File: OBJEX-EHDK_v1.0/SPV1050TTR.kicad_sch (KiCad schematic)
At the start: 14 parts

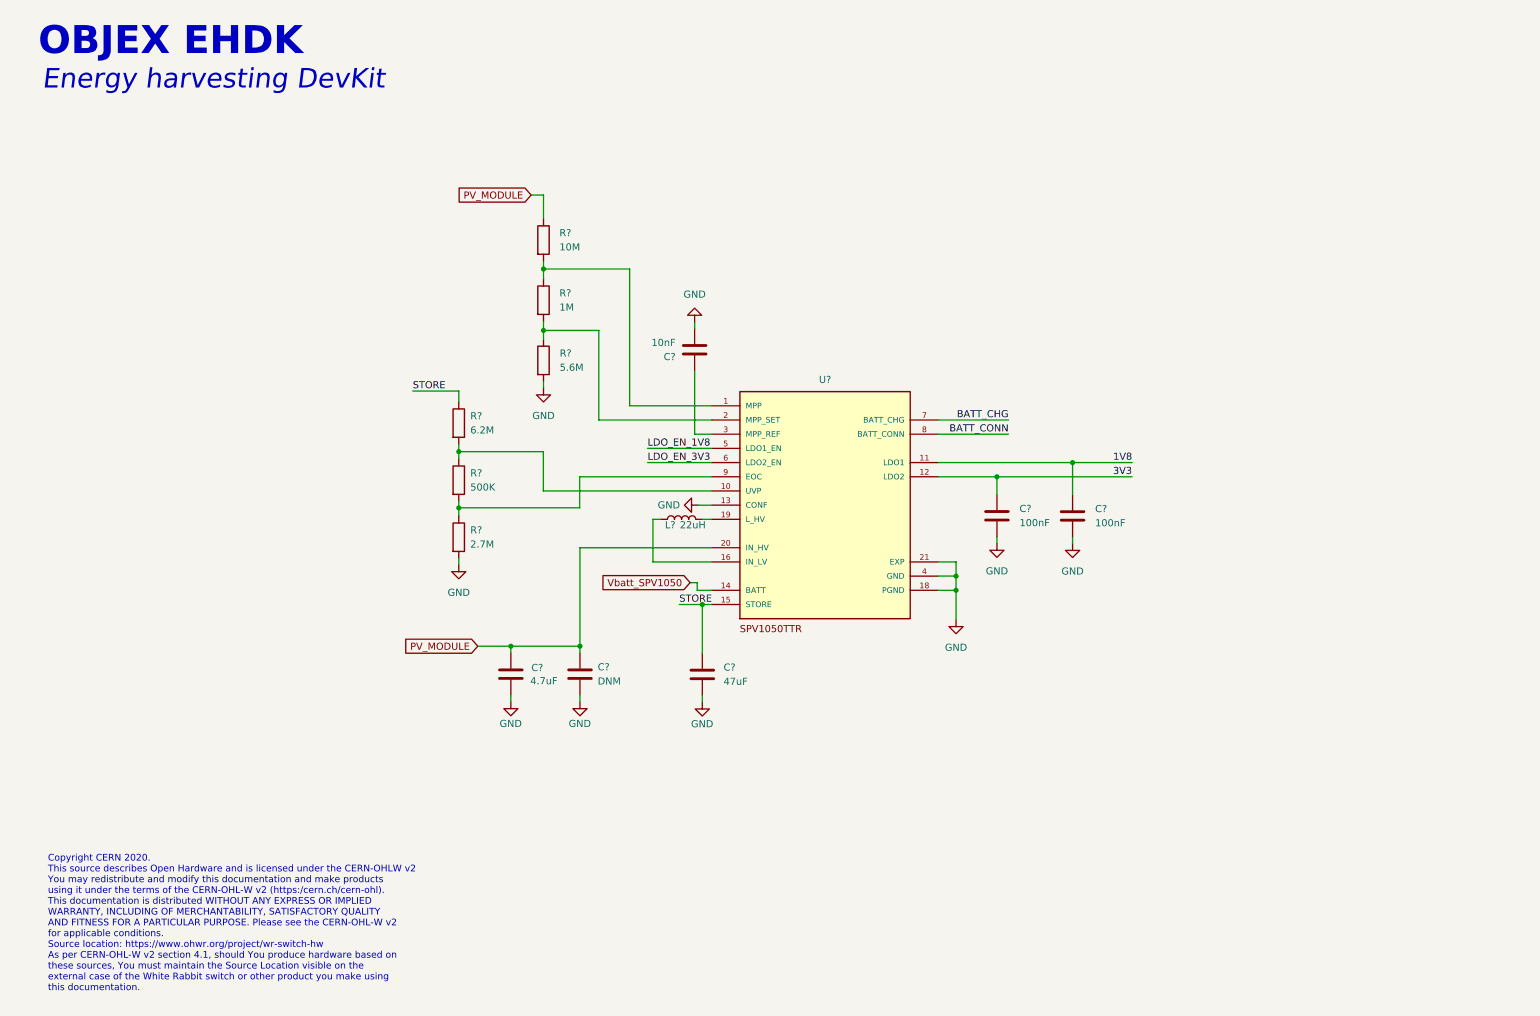
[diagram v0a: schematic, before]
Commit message: Update design, EH ICs & Battery conn
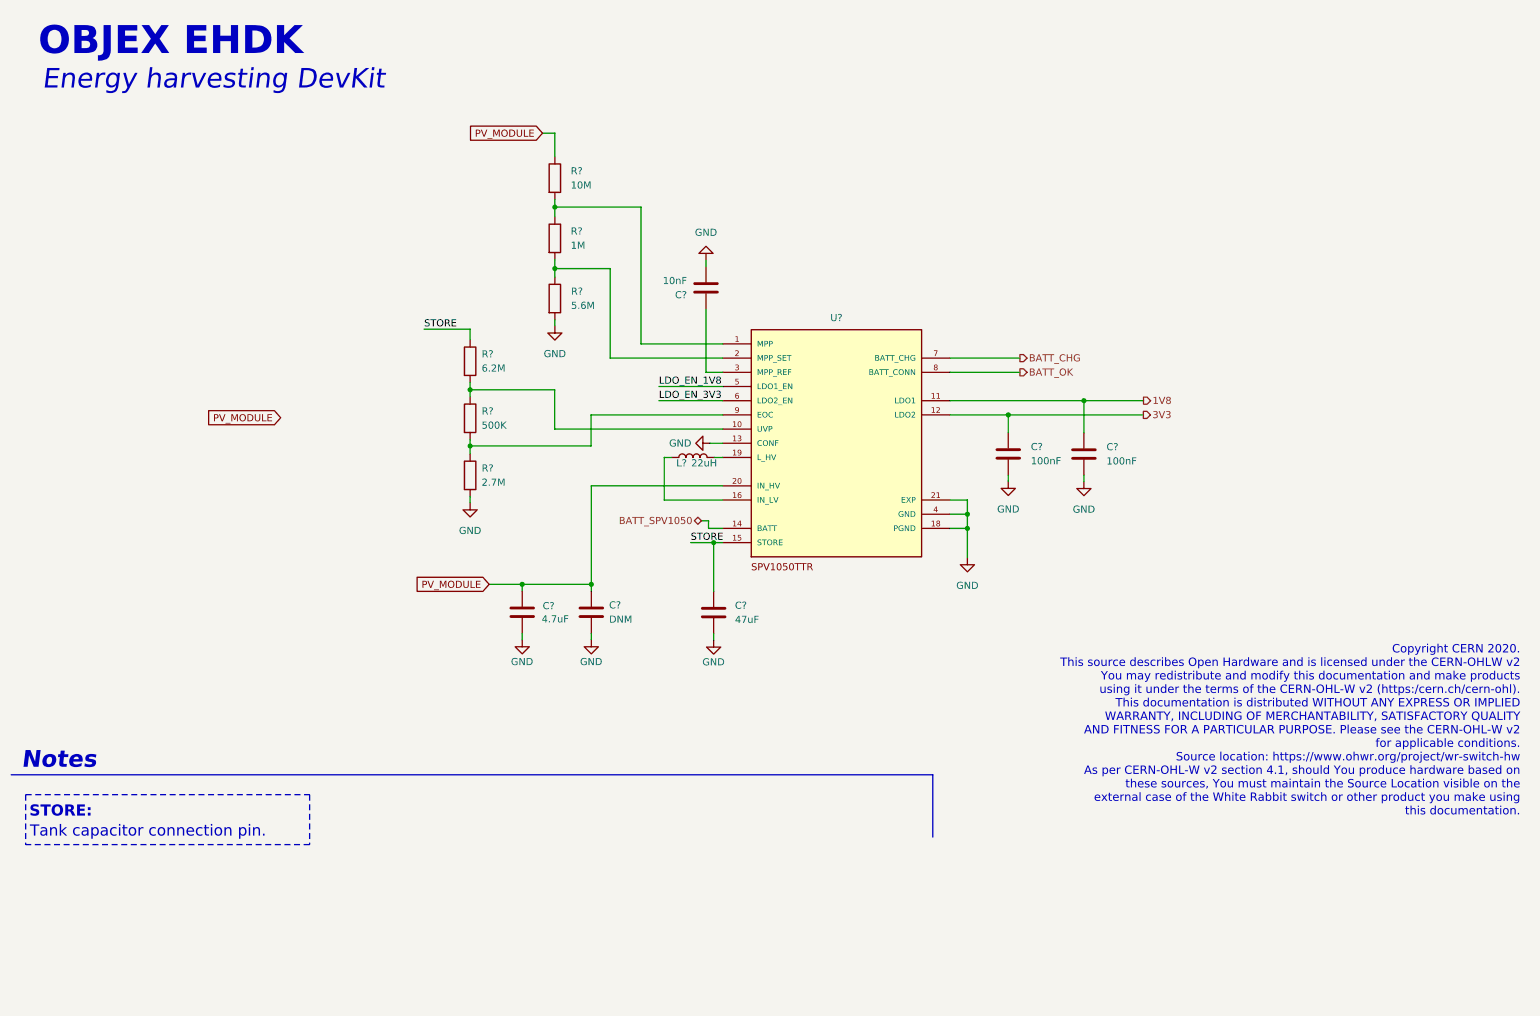
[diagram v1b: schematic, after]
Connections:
- net BATT_CONN renamed BATT_OK
- net Vbatt_SPV1050 renamed BATT_SPV1050
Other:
- note added: "Notes"
- note added: "STORE:"
- note added: "Tank capacitor connection pin."
- moved on the sheet: C?, L?, R?, U?

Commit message: update sch
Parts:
- added J?: Conn_01x05, symbol Connector_Generic:Conn_01x05
- added J?: Solar, symbol Connector_Generic:Conn_01x02
- added J?: 3V3, symbol Connector_Generic:Conn_01x02
- added J?: 1V8, symbol Connector_Generic:Conn_01x02
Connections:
- net BATT_CHG: now also J?.2 (Pin_2)
- net BATT_OK: now also J?.1 (Pin_1)
- net GND: now also J?.1 (Pin_1), J?.2 (Pin_2), J?.2 (Pin_2)
- net LDO_EN_1V8: now also J?.3 (Pin_3)
- net LDO_EN_3V3: now also J?.4 (Pin_4)
- net PV_MODULE: now also J?.2 (Pin_2)
- net STORE: now also J?.5 (Pin_5)
- net 1V8: no longer names the net of C?.1, U?.11 (LDO1)
- net 1V8: now also J?.1 (Pin_1)
- net 3V3: no longer names the net of C?.1, U?.12 (LDO2)
- net 3V3: now also J?.1 (Pin_1)
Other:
- note added: "OUTPUT"

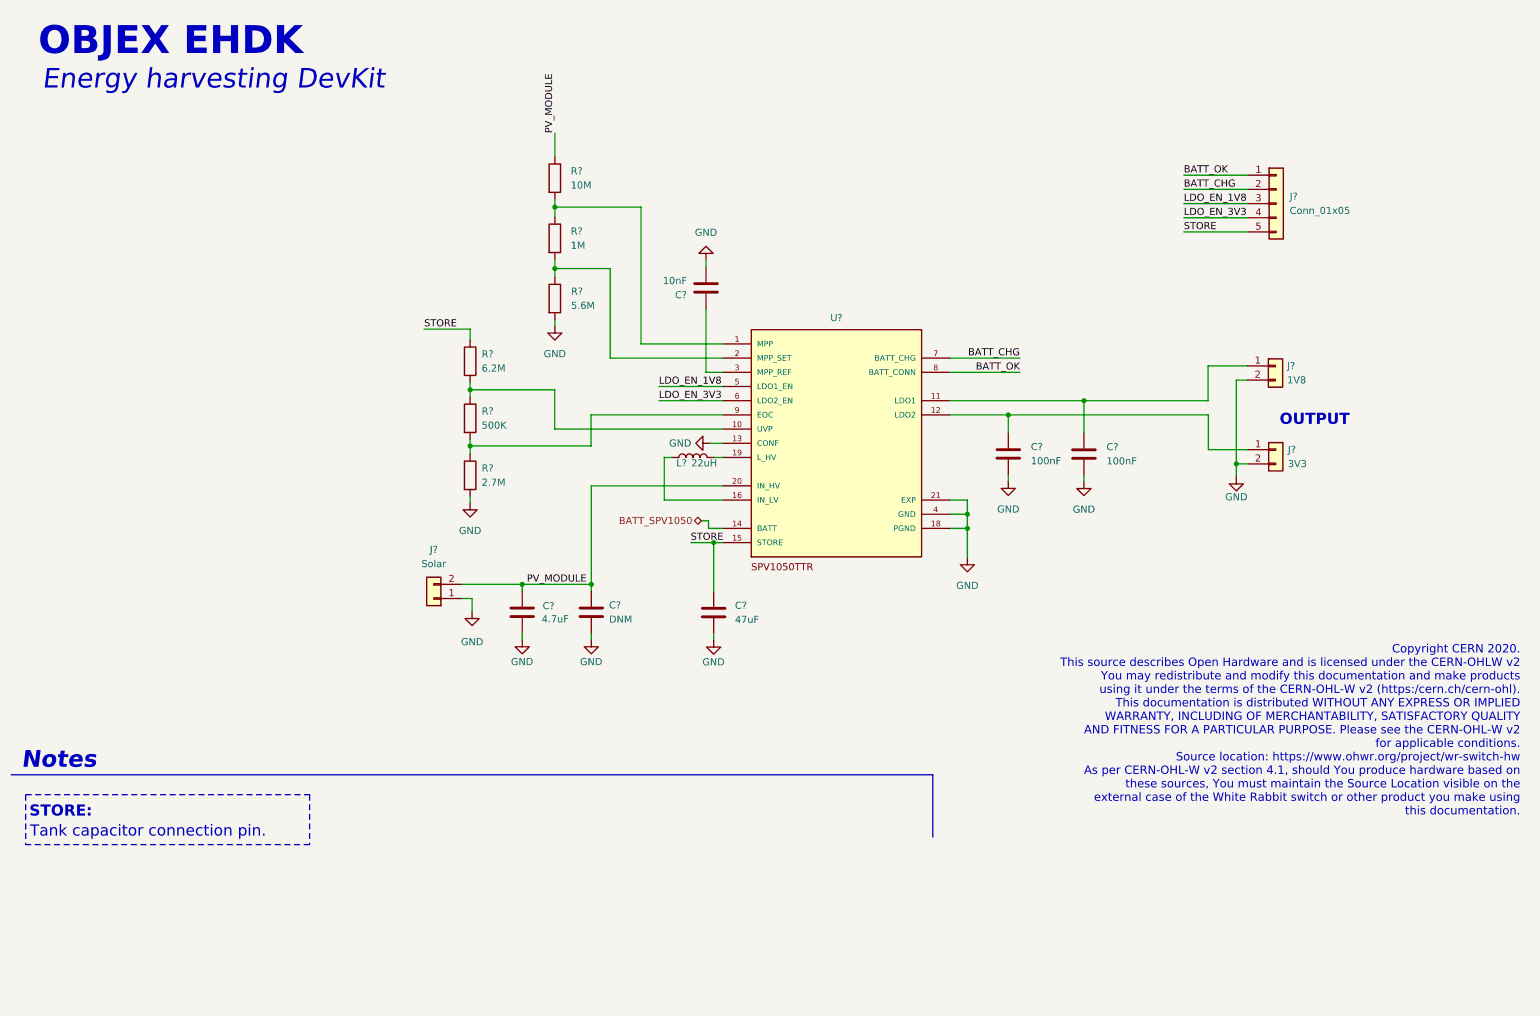
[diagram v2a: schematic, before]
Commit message: Fix, add test points
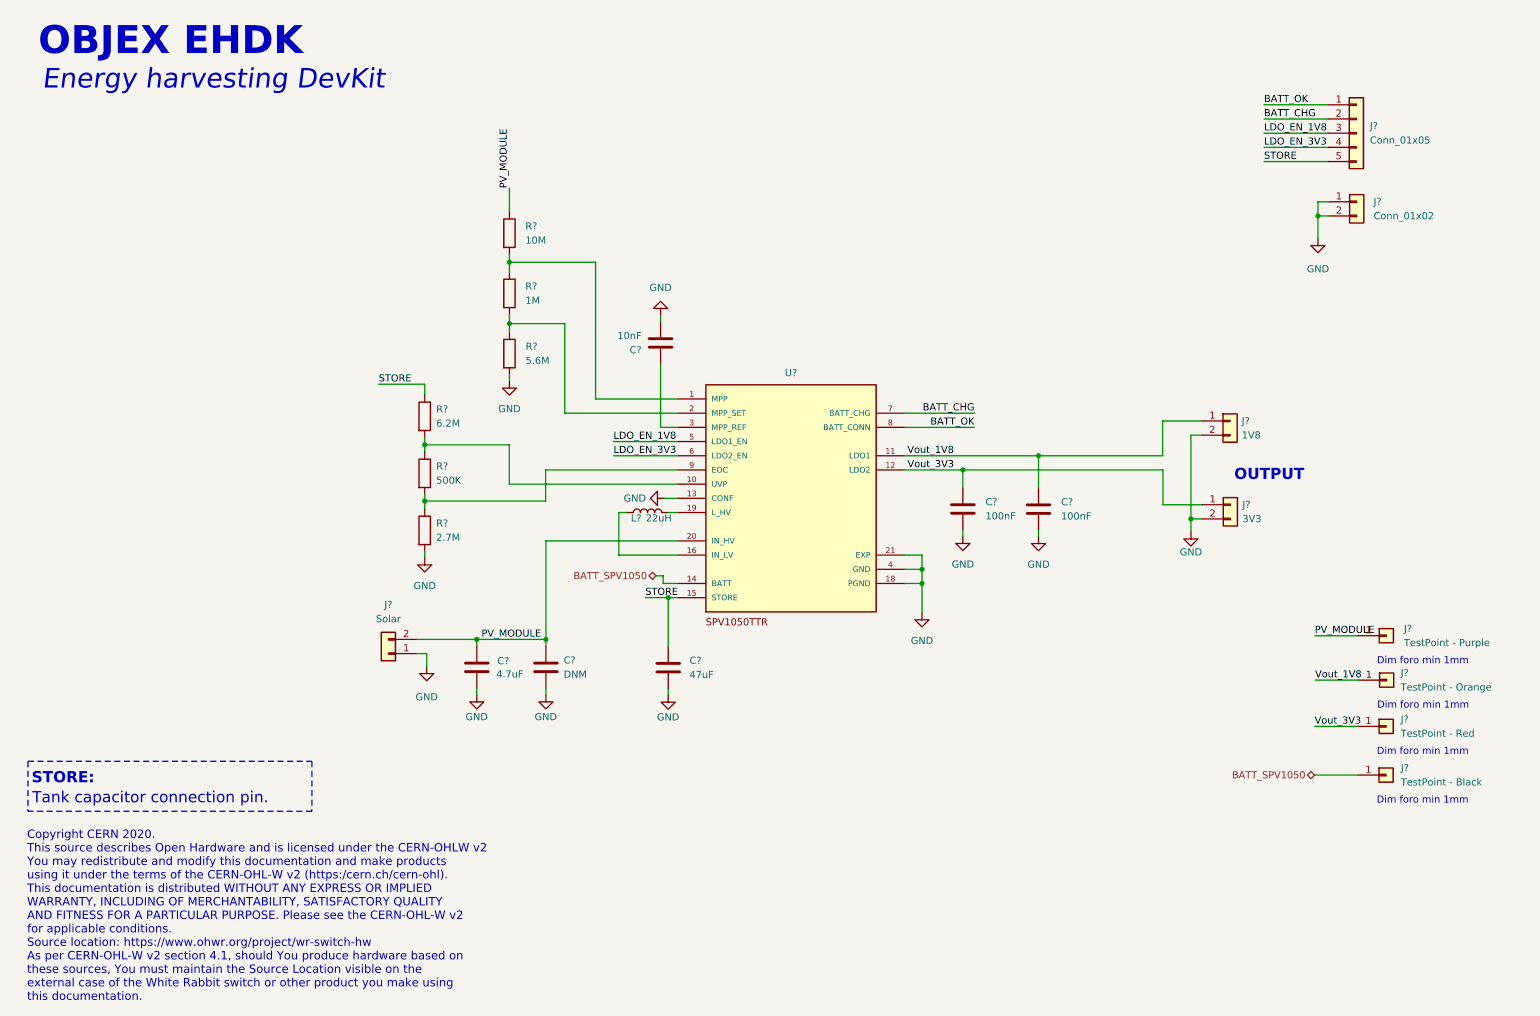
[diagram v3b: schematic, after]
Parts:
- added J?: TestPoint - Red, symbol Connector_Generic:Conn_01x01
- added J?: Conn_01x02, symbol Connector_Generic:Conn_01x02
- added J?: TestPoint - Purple, symbol Connector_Generic:Conn_01x01
- added J?: TestPoint - Orange, symbol Connector_Generic:Conn_01x01
- added J?: TestPoint - Black, symbol Connector_Generic:Conn_01x01
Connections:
- net BATT_SPV1050: now also J?.1 (Pin_1)
- net GND: now also J?.1 (Pin_1), J?.2 (Pin_2)
- net PV_MODULE: now also J?.1 (Pin_1)
- net Vout_1V8: now reaches C?.1, J?.1 (Pin_1), U?.11 (LDO1)
- net Vout_1V8: now also J?.1 (Pin_1)
- net Vout_3V3: now reaches C?.1, J?.1 (Pin_1), U?.12 (LDO2)
- net Vout_3V3: now also J?.1 (Pin_1)
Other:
- note added: "Dim foro min 1mm"
- note removed: "Notes"
- moved on the sheet: C?, J?, L?, R?, U?

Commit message: SCH Ready for first review
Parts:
- C1: renamed from C?; value 4.7uF -> 4.7uF/25V; footprint (none) -> Capacitor_SMD:C_0603_1608Metric
- C2: renamed from C?; footprint (none) -> Capacitor_SMD:C_0603_1608Metric
- C3, C5, C6: renamed from C?; footprint (none) -> Capacitor_SMD:C_0402_1005Metric
- C4: renamed from C?; value 47uF -> 47uF/10V; footprint (none) -> Capacitor_SMD:C_0805_2012Metric
- J10, J6, J7, J8: renamed from J?; footprint (none) -> Connector_PinHeader_2.54mm:PinHeader_1x02_P2.54mm_Vertical
- J11, J12, J13, J14: renamed from J?; footprint (none) -> TestPoint:TestPoint_Loop_D3.80mm_Drill2.0mm
- J9: renamed from J?; footprint (none) -> Connector_PinHeader_2.54mm:PinHeader_1x05_P2.54mm_Vertical
- L1: renamed from L?; footprint (none) -> Inductor_SMD:L_0603_1608Metric
- R1, R2, R3, R4, R5, R6: renamed from R?; footprint (none) -> Resistor_SMD:R_0603_1608Metric
- U1: renamed from U?; footprint QFN40P300X300X100-21N -> lib:QFN40P300X300X100-21N
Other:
- moved on the sheet: C1, J6

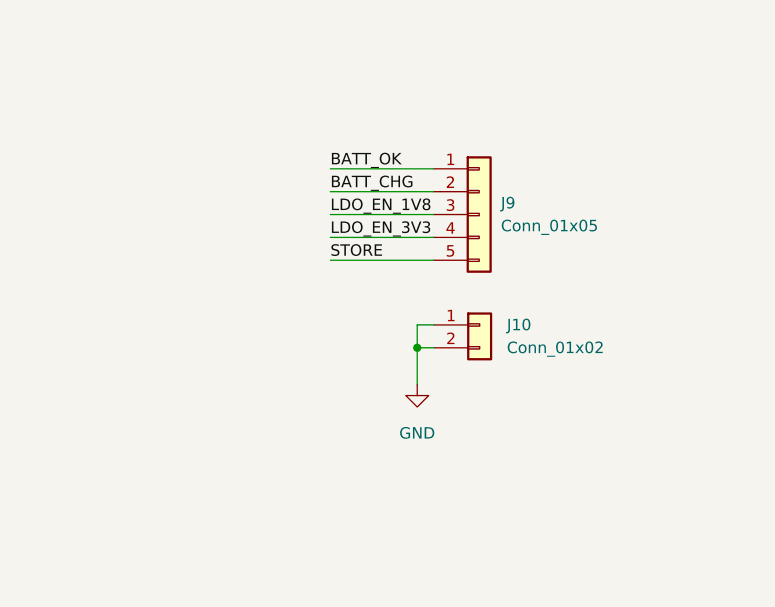
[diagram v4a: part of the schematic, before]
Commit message: SCH Ready for PCB design
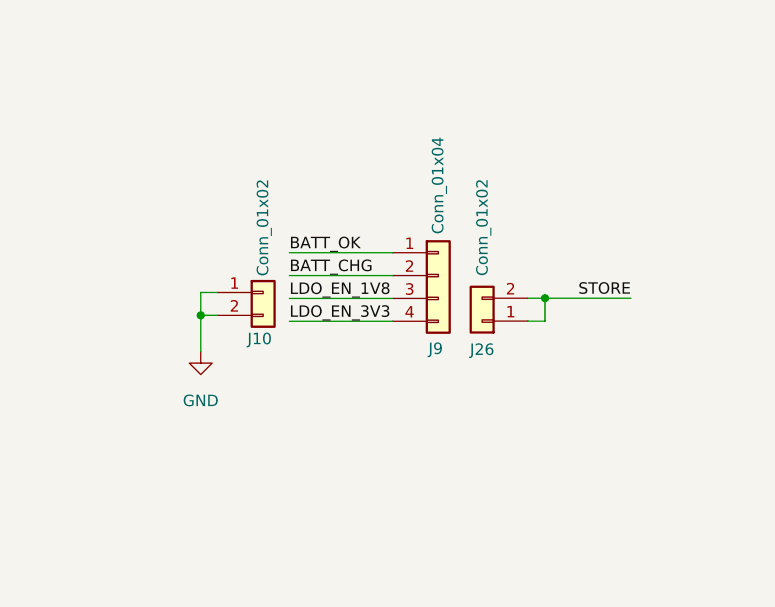
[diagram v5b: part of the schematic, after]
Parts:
- removed J9: Conn_01x05, Connector_PinHeader_2.54mm:PinHeader_1x05_P2.54mm_Vertical, symbol Connector_Generic:Conn_01x05
- added J26: Conn_01x02, Connector_PinHeader_2.54mm:PinHeader_1x02_P2.54mm_Vertical, symbol Connector_Generic:Conn_01x02
- added J9: Conn_01x04, Connector_PinHeader_2.54mm:PinHeader_1x04_P2.54mm_Vertical, symbol Connector_Generic:Conn_01x04
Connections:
- net BATT_CHG: now also J9.2 (Pin_2)
- net BATT_OK: now also J9.1 (Pin_1)
- net LDO_EN_1V8: now also J9.3 (Pin_3)
- net LDO_EN_3V3: now also J9.4 (Pin_4)
- net STORE: now also J26.1 (Pin_1), J26.2 (Pin_2)
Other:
- moved on the sheet: J10
